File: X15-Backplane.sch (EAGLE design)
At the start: 35 parts, among them J3 IPL1-103-01-L-S-K, J4 IPL1-104-01-X-S-K

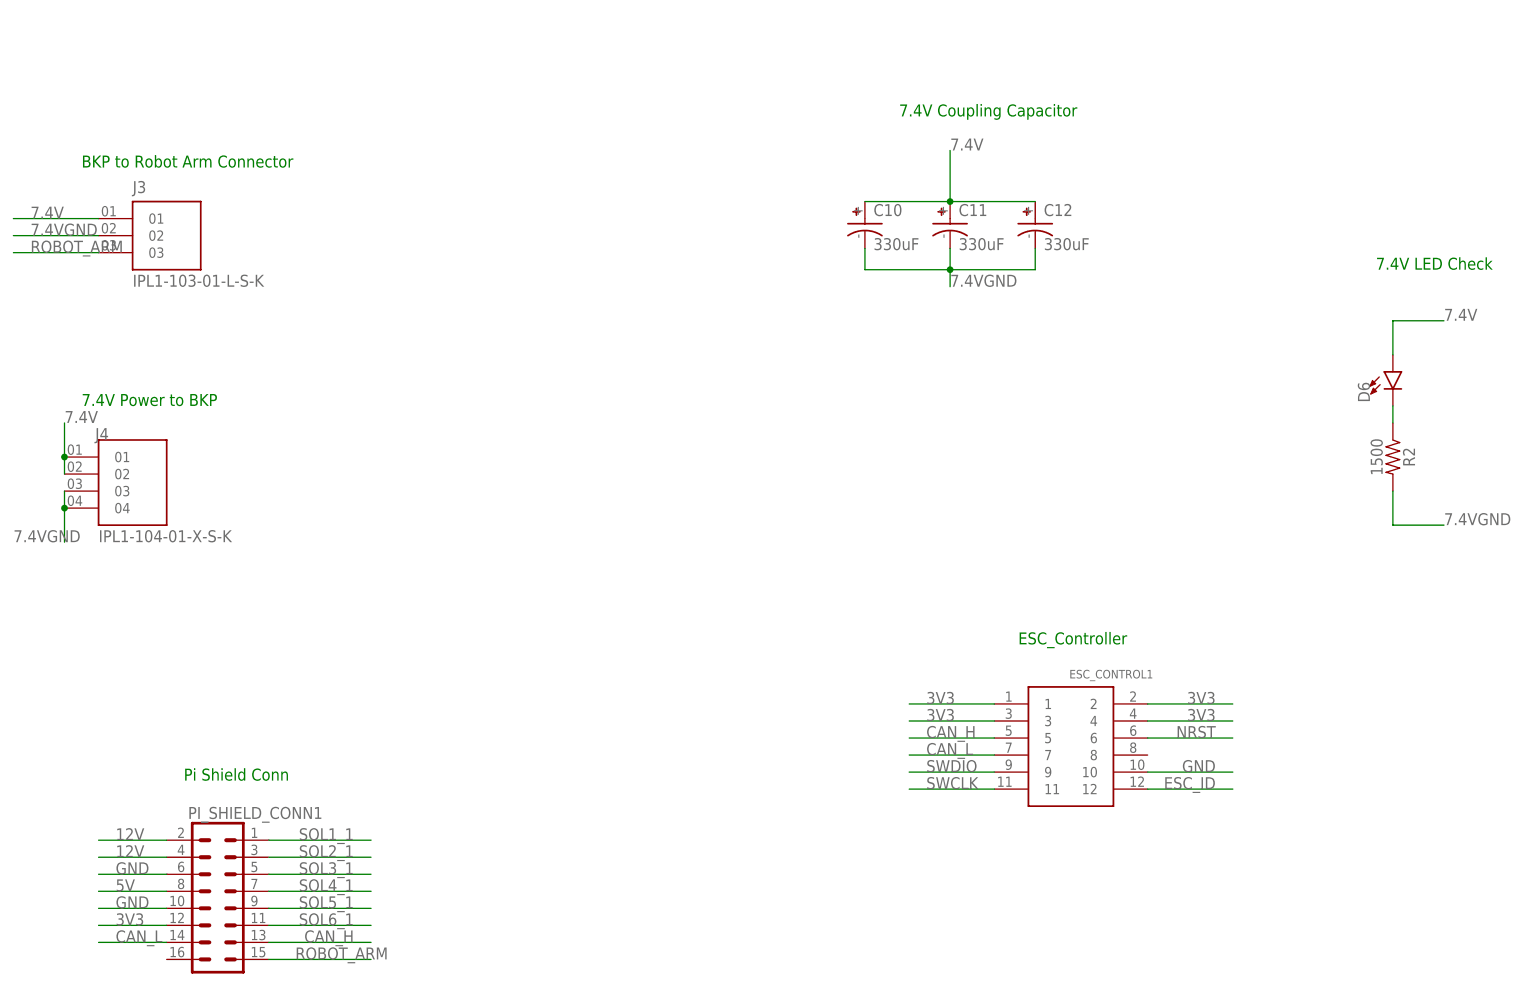
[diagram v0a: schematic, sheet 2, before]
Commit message: LED Added
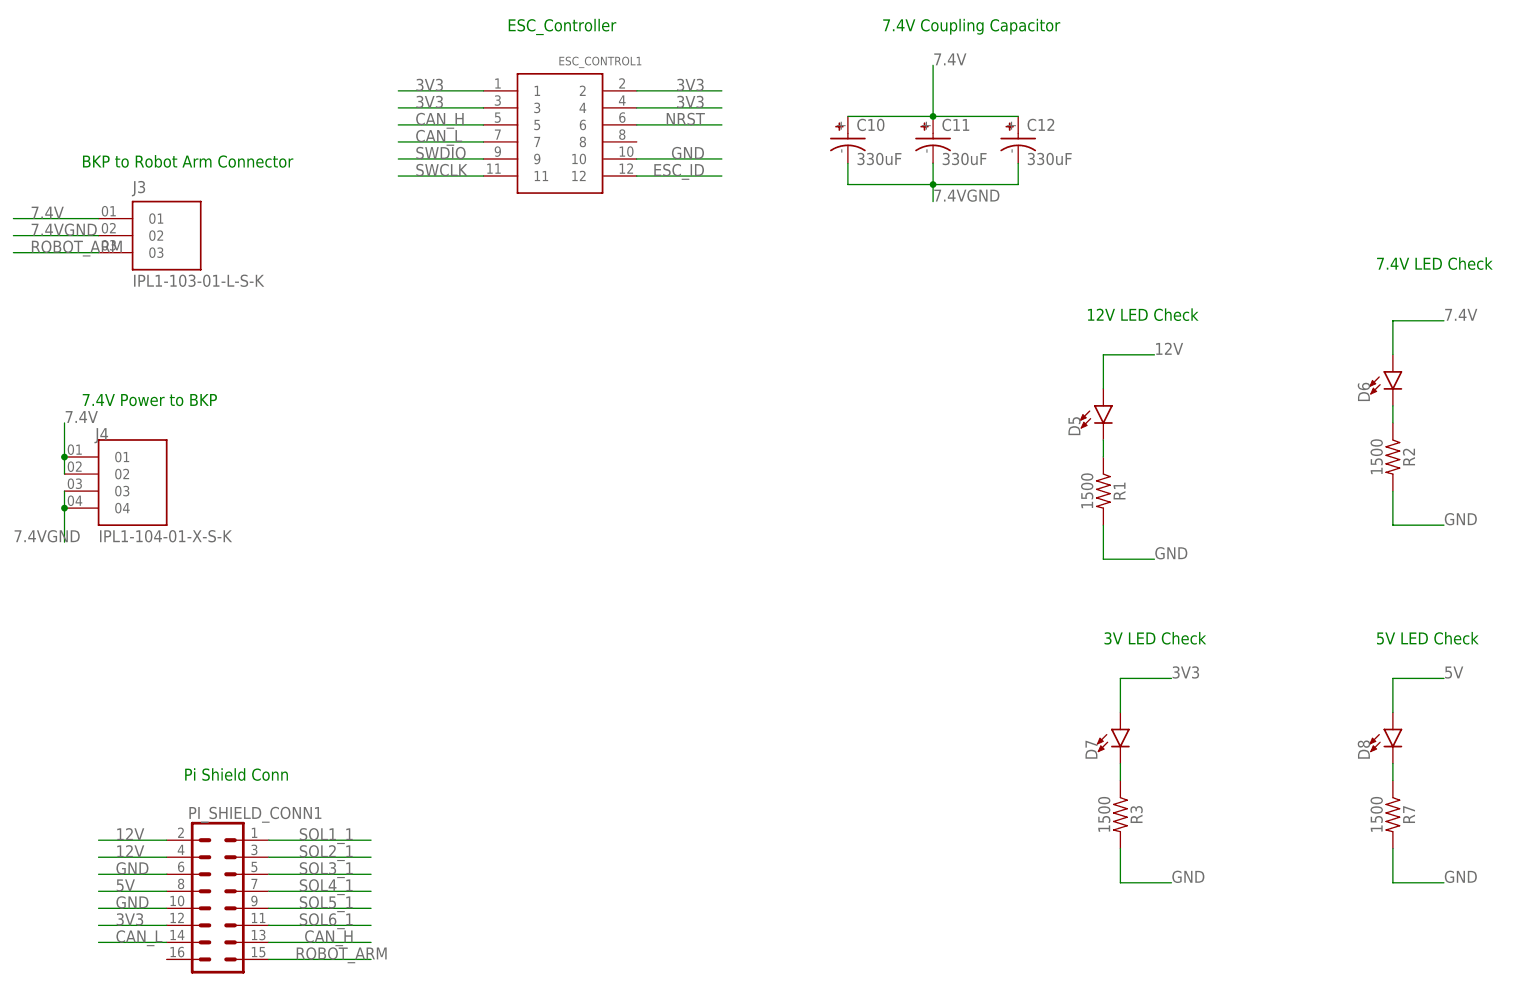
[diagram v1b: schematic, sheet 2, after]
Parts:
- added D5, D7, D8: (no value), SparkFun-LED:LED3MM
- added R1, R3, R7: 1500, SparkFun-Resistors:RESISTOR0603
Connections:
- new net N$2: D5.C, R1.1
- new net N$3: D7.C, R3.1
- new net N$5: D8.C, R7.1
- net 12V: now also D5.A
- net 3V3: now also D7.A
- net 5V: now also D8.A
- net 7.4VGND: no longer R2.2
- net GND: now also R1.2, R2.2, R3.2, R7.2
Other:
- note added: "12V LED Check"
- note added: "3V LED Check"
- note added: "5V LED Check"
- moved on the sheet: C10, C11, C12, ESC_CONTROL1

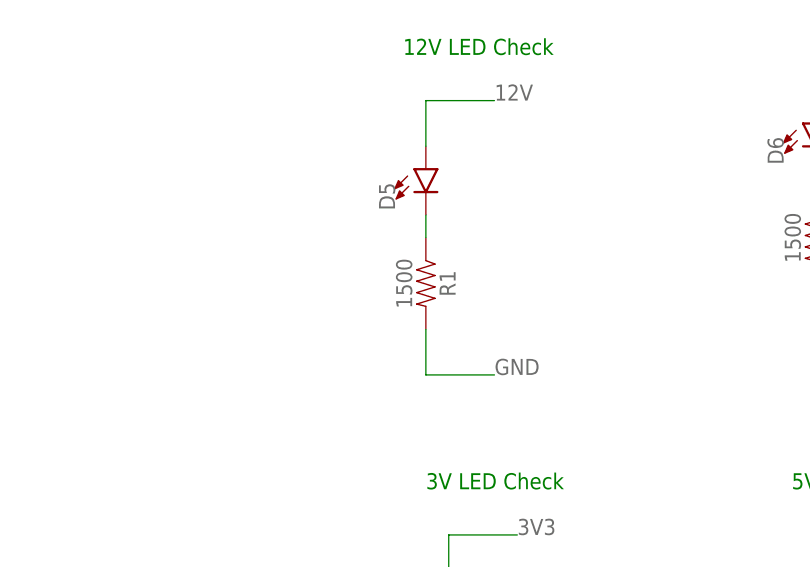
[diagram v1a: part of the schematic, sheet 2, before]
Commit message: LED Added
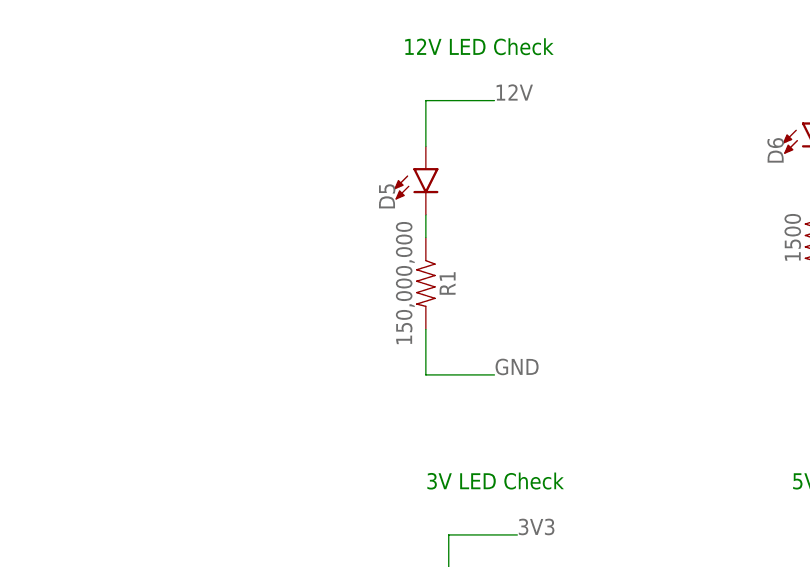
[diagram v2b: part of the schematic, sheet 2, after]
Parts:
- R1: value 1500 -> 150,000,000
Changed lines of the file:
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@@
 <part name="J4" library="X15-Backplane Parts" deviceset="IPL1-104-01-X-S-K" device=""/>
 <part name="D5" library="SparkFun-LED" library_urn="urn:adsk.eagle:library:529" deviceset="LED" device="3MM" package3d_urn="urn:adsk.eagle:package:39361/1"/>
-<part name="R1" library="SparkFun-Resistors" library_urn="urn:adsk.eagle:library:532" deviceset="RESISTOR" device="0603" package3d_urn="urn:adsk.eagle:package:39650/1" value="1500"/>
+<part name="R1" library="SparkFun-Resistors" library_urn="urn:adsk.eagle:library:532" deviceset="RESISTOR" device="0603" package3d_urn="urn:adsk.eagle:package:39650/1" value="150,000,000"/>
 <part name="D7" library="SparkFun-LED" library_urn="urn:adsk.eagle:library:529" deviceset="LED" device="3MM" package3d_urn="urn:adsk.eagle:package:39361/1"/>
 <part name="R3" library="SparkFun-Resistors" library_urn="urn:adsk.eagle:library:532" deviceset="RESISTOR" device="0603" package3d_urn="urn:adsk.eagle:package:39650/1" value="1500"/>
